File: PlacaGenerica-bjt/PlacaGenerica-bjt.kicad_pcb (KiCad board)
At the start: 2 copper layers, 30.5 x 29.6 mm, 13 parts, among them J1 Screw_Terminal_01x01, J2 Screw_Terminal_01x01, J3 Screw_Terminal_01x01, J4 Screw_Terminal_01x01, Q1 BC337

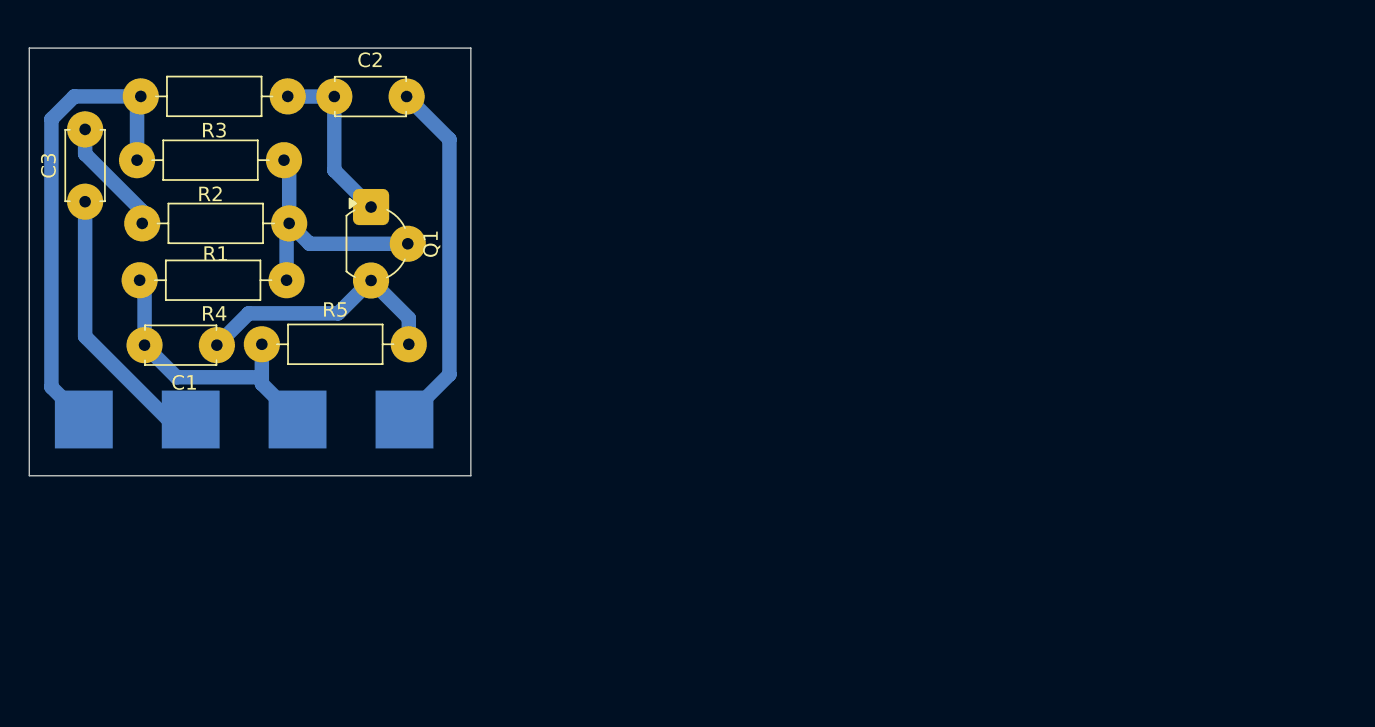
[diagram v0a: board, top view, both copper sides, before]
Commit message: Actualiza PlacaGenerica-bjt para todos los lab
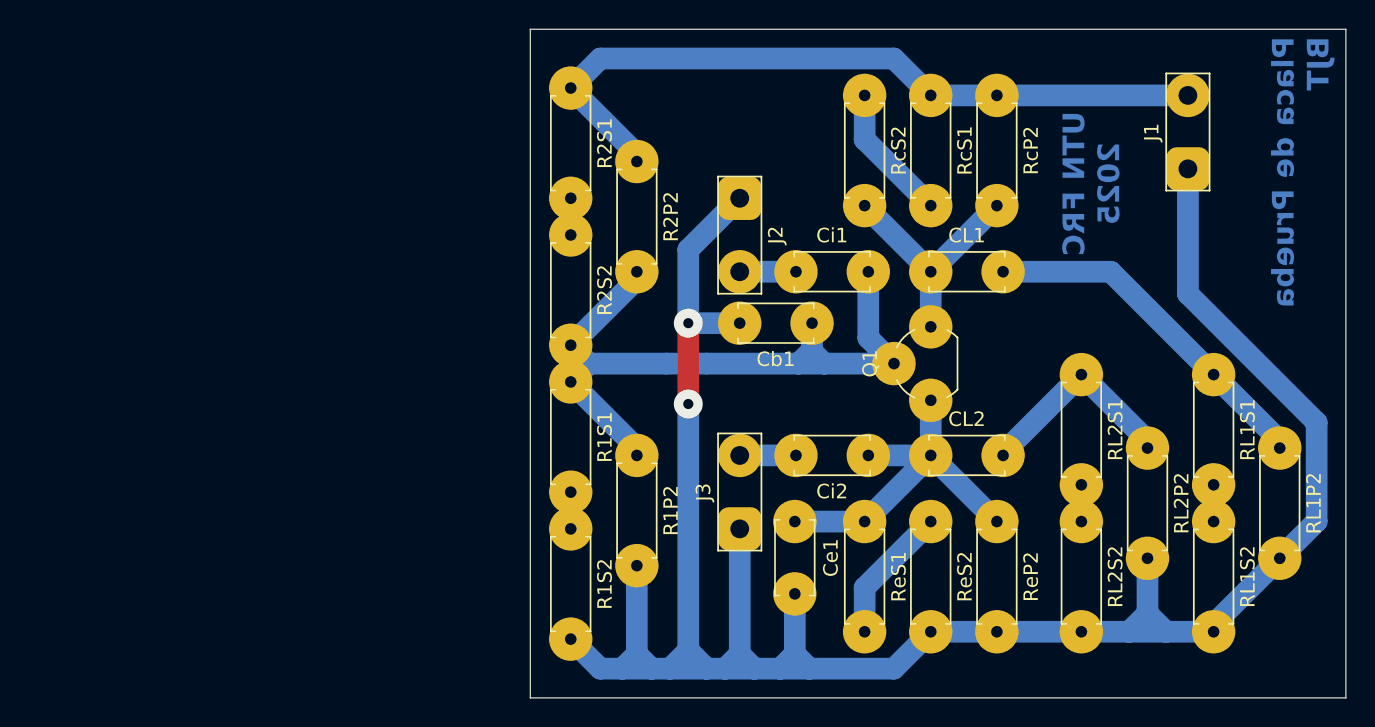
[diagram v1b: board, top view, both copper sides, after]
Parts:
- removed C1, C2, C3: C, Capacitor_THT:C_Disc_D4.7mm_W2.5mm_P5.00mm
- removed J4: Screw_Terminal_01x01, TestPoint:TestPoint_Pad_4.0x4.0mm
- removed R1, R2, R3, R4, R5: R, Resistor_THT:R_Axial_DIN0207_L6.3mm_D2.5mm_P10.16mm_Horizontal
- added CL1: C, Capacitor_THT:C_Disc_D5.0mm_W2.5mm_P5.00mm, F.Cu at (147.8, 65.0)
- added CL2: C, Capacitor_THT:C_Disc_D5.0mm_W2.5mm_P5.00mm, F.Cu at (147.8, 77.7)
- added Cb1: C, Capacitor_THT:C_Disc_D5.0mm_W2.5mm_P5.00mm, F.Cu at (139.6, 68.6)
- added Ce1: C, Capacitor_THT:C_Disc_D5.0mm_W2.5mm_P5.00mm, F.Cu at (138.4, 82.3)
- added Ci1: C, Capacitor_THT:C_Disc_D5.0mm_W2.5mm_P5.00mm, F.Cu at (138.5, 65.0)
- added Ci2: C, Capacitor_THT:C_Disc_D5.0mm_W2.5mm_P5.00mm, F.Cu at (143.5, 77.7)
- added R1P2: R, Resistor_THT:R_Axial_DIN0207_L6.3mm_D2.5mm_P7.62mm_Horizontal, F.Cu at (127.5, 77.7)
- added R1S1: R, Resistor_THT:R_Axial_DIN0207_L6.3mm_D2.5mm_P7.62mm_Horizontal, F.Cu at (122.9, 72.6)
- added R1S2: R, Resistor_THT:R_Axial_DIN0207_L6.3mm_D2.5mm_P7.62mm_Horizontal, F.Cu at (122.9, 82.8)
- added R2P2: R, Resistor_THT:R_Axial_DIN0207_L6.3mm_D2.5mm_P7.62mm_Horizontal, F.Cu at (127.5, 57.4)
- added R2S1: R, Resistor_THT:R_Axial_DIN0207_L6.3mm_D2.5mm_P7.62mm_Horizontal, F.Cu at (122.9, 52.3)
- added R2S2: R, Resistor_THT:R_Axial_DIN0207_L6.3mm_D2.5mm_P7.62mm_Horizontal, F.Cu at (122.9, 62.5)
- added RL1P2: R, Resistor_THT:R_Axial_DIN0207_L6.3mm_D2.5mm_P7.62mm_Horizontal, F.Cu at (172.0, 77.2)
- added RL1S1: R, Resistor_THT:R_Axial_DIN0207_L6.3mm_D2.5mm_P7.62mm_Horizontal, F.Cu at (167.4, 72.1)
- added RL1S2: R, Resistor_THT:R_Axial_DIN0207_L6.3mm_D2.5mm_P7.62mm_Horizontal, F.Cu at (167.4, 82.3)
- added RL2P2: R, Resistor_THT:R_Axial_DIN0207_L6.3mm_D2.5mm_P7.62mm_Horizontal, F.Cu at (162.8, 77.2)
- added RL2S1: R, Resistor_THT:R_Axial_DIN0207_L6.3mm_D2.5mm_P7.62mm_Horizontal, F.Cu at (158.2, 72.1)
- added RL2S2: R, Resistor_THT:R_Axial_DIN0207_L6.3mm_D2.5mm_P7.62mm_Horizontal, F.Cu at (158.2, 82.3)
- added RcP2: R, Resistor_THT:R_Axial_DIN0207_L6.3mm_D2.5mm_P7.62mm_Horizontal, F.Cu at (152.4, 52.8)
- added RcS1: R, Resistor_THT:R_Axial_DIN0207_L6.3mm_D2.5mm_P7.62mm_Horizontal, F.Cu at (147.8, 52.8)
- added RcS2: R, Resistor_THT:R_Axial_DIN0207_L6.3mm_D2.5mm_P7.62mm_Horizontal, F.Cu at (143.3, 52.8)
- added ReP2: R, Resistor_THT:R_Axial_DIN0207_L6.3mm_D2.5mm_P7.62mm_Horizontal, F.Cu at (152.4, 82.3)
- added ReS1: R, Resistor_THT:R_Axial_DIN0207_L6.3mm_D2.5mm_P7.62mm_Horizontal, F.Cu at (143.3, 82.3)
- added ReS2: R, Resistor_THT:R_Axial_DIN0207_L6.3mm_D2.5mm_P7.62mm_Horizontal, F.Cu at (147.8, 82.3)
- J1: value Screw_Terminal_01x01 -> Vcc; footprint TestPoint:TestPoint_Pad_4.0x4.0mm -> TestPoint:TestPoint_2Pads_Pitch5.08mm_Drill1.3mm; moved to F.Cu
- J2: value Screw_Terminal_01x01 -> Vin1; footprint TestPoint:TestPoint_Pad_4.0x4.0mm -> TestPoint:TestPoint_2Pads_Pitch5.08mm_Drill1.3mm; moved to F.Cu
- J3: value Screw_Terminal_01x01 -> Vin2; footprint TestPoint:TestPoint_Pad_4.0x4.0mm -> TestPoint:TestPoint_2Pads_Pitch5.08mm_Drill1.3mm; moved to F.Cu
- Q1: value BC337 -> NPN; footprint Package_TO_SOT_THT:TO-92L_Wide -> Package_TO_SOT_THT:TO-92_Wide
- moved J1 71.1 mm to (165.6, 57.9), turned to 90 degrees
- moved J2 47.9 mm to (134.6, 59.9), turned to -90 degrees
- moved Q1 40.9 mm to (147.8, 73.9), turned to 90 degrees
- moved J3 24.4 mm to (134.6, 82.8), turned to 90 degrees
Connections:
- J1 pad 1: VAC -> GND
- J2 pad 1: VCC -> GND
- J3 pad 1: VOUT -> GND
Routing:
- net GND: track 19.3 -> 159.9 mm, vias 0 -> 2
- net Net-(Q1-B): track 17.3 -> 52.7 mm
- net VOUT: track 24.8 -> 0.00 mm
- net Net-(CL1-Pad2): track 0.00 -> 24.5 mm
- net VAC: track 19.0 -> 0.00 mm
- net VCC: track 33.0 -> 51.5 mm
- net Net-(CL2-Pad2): track 0.00 -> 14.8 mm
- net Net-(RcS1-Pad2): track 0.00 -> 9.51 mm
- net Net-(ReS1-Pad2): track 0.00 -> 9.51 mm
- net Net-(C3-Pad2): track 8.14 -> 0.00 mm
- net Net-(Q1-E): track 18.0 -> 25.9 mm
- net Net-(Q1-C): track 11.9 -> 16.7 mm
- net VIN2: track 0.00 -> 3.89 mm
- net VIN1: track 0.00 -> 3.89 mm
- net Net-(RL2S1-Pad2): track 0.00 -> 2.54 mm
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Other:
- board size 30.5 x 29.6 mm -> 56.4 x 46.2 mm
- board text added: "Placa de Prueba BJT"
- board text added: "UTN FRC 2025"

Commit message: Agrega serigrafia visual a PlacaGenerica-bjt
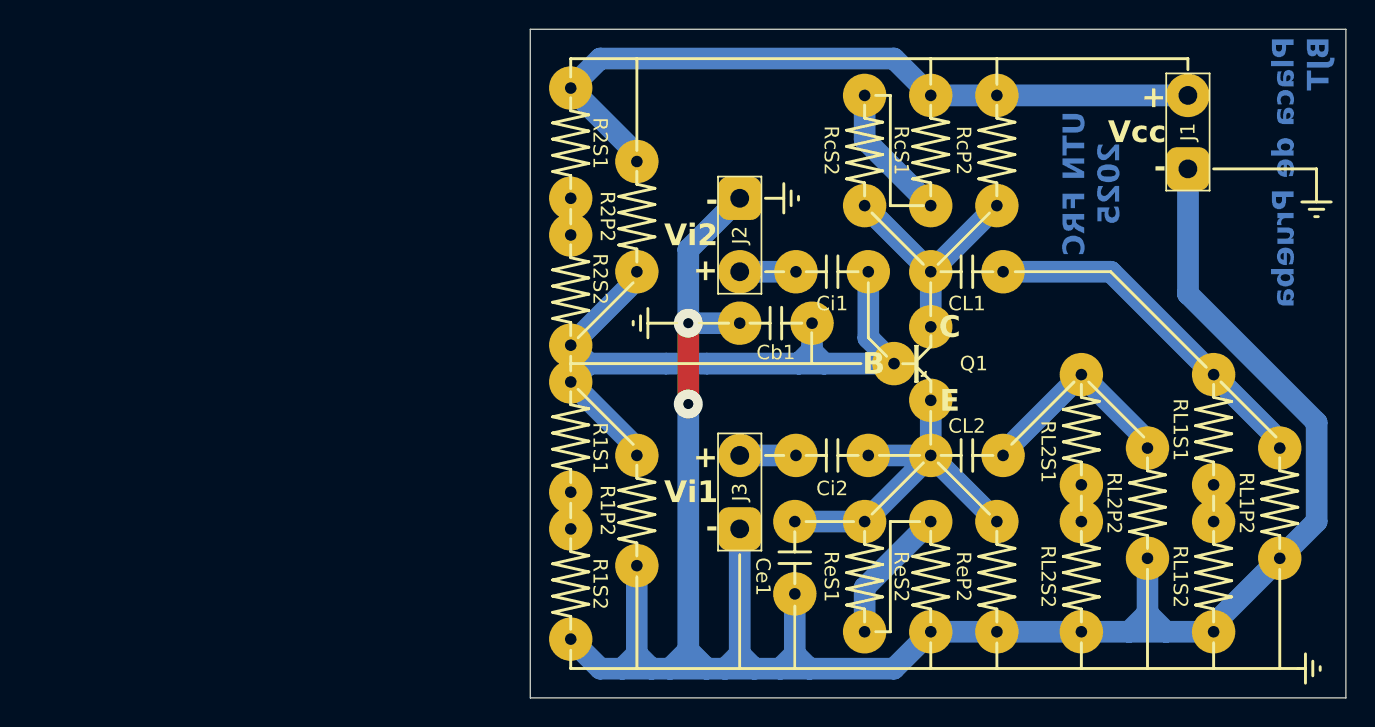
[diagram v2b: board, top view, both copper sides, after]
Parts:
- CL1, CL2, Cb1, Ce1, Ci1, Ci2: footprint Capacitor_THT:C_Disc_D5.0mm_W2.5mm_P5.00mm -> PrettyFootprints:Pretty-C_Disc_D5.0mm_W2.5mm_P5.00mm
- Q1: footprint Package_TO_SOT_THT:TO-92_Wide -> PrettyFootprints:Pretty-TO-92_Wide
- R1P2, R1S1, R1S2, R2P2, R2S1, R2S2, RL1P2, RL1S1, RL1S2, RL2P2, RL2S1, RL2S2, RcP2, RcS1, RcS2, ReP2, ReS1, ReS2: footprint Resistor_THT:R_Axial_DIN0207_L6.3mm_D2.5mm_P7.62mm_Horizontal -> PrettyFootprints:Pretty-R_Axial_DIN0207_L6.3mm_D2.5mm_P7.62mm_Horizontal
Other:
- board text added: "+ Vcc -"
- board text added: "+ Vi1 -"
- board text added: "- Vi2 +"
